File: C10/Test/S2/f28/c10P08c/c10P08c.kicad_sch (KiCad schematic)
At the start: 2 parts

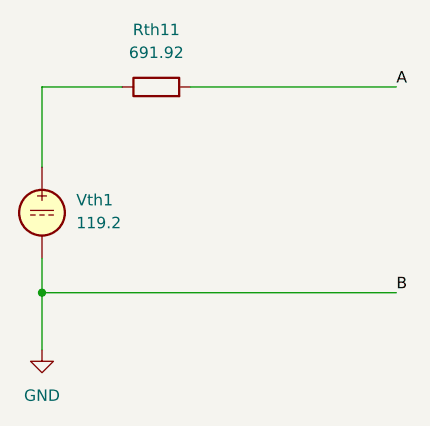
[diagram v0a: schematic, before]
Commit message: corrected from misprinting Fig 10-28
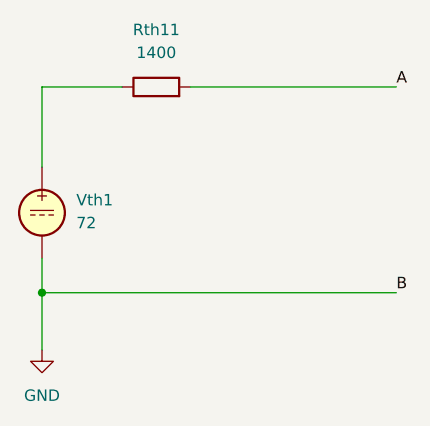
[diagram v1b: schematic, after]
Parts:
- Rth11: value 691.92 -> 1400
- Vth1: value 119.2 -> 72
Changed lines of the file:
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@@
 			)
 		)
-		(property "Value" "119.2"
+		(property "Value" "72"
 			(at 139.7 87.5001 0)
 			(show_name no)
@@
 			)
 		)
-		(property "Value" "691.92"
+		(property "Value" "1400"
 			(at 148.59 68.58 90)
 			(show_name no)
